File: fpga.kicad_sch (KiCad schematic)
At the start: 14 parts, among them U1 XC6SLX25-FTG256

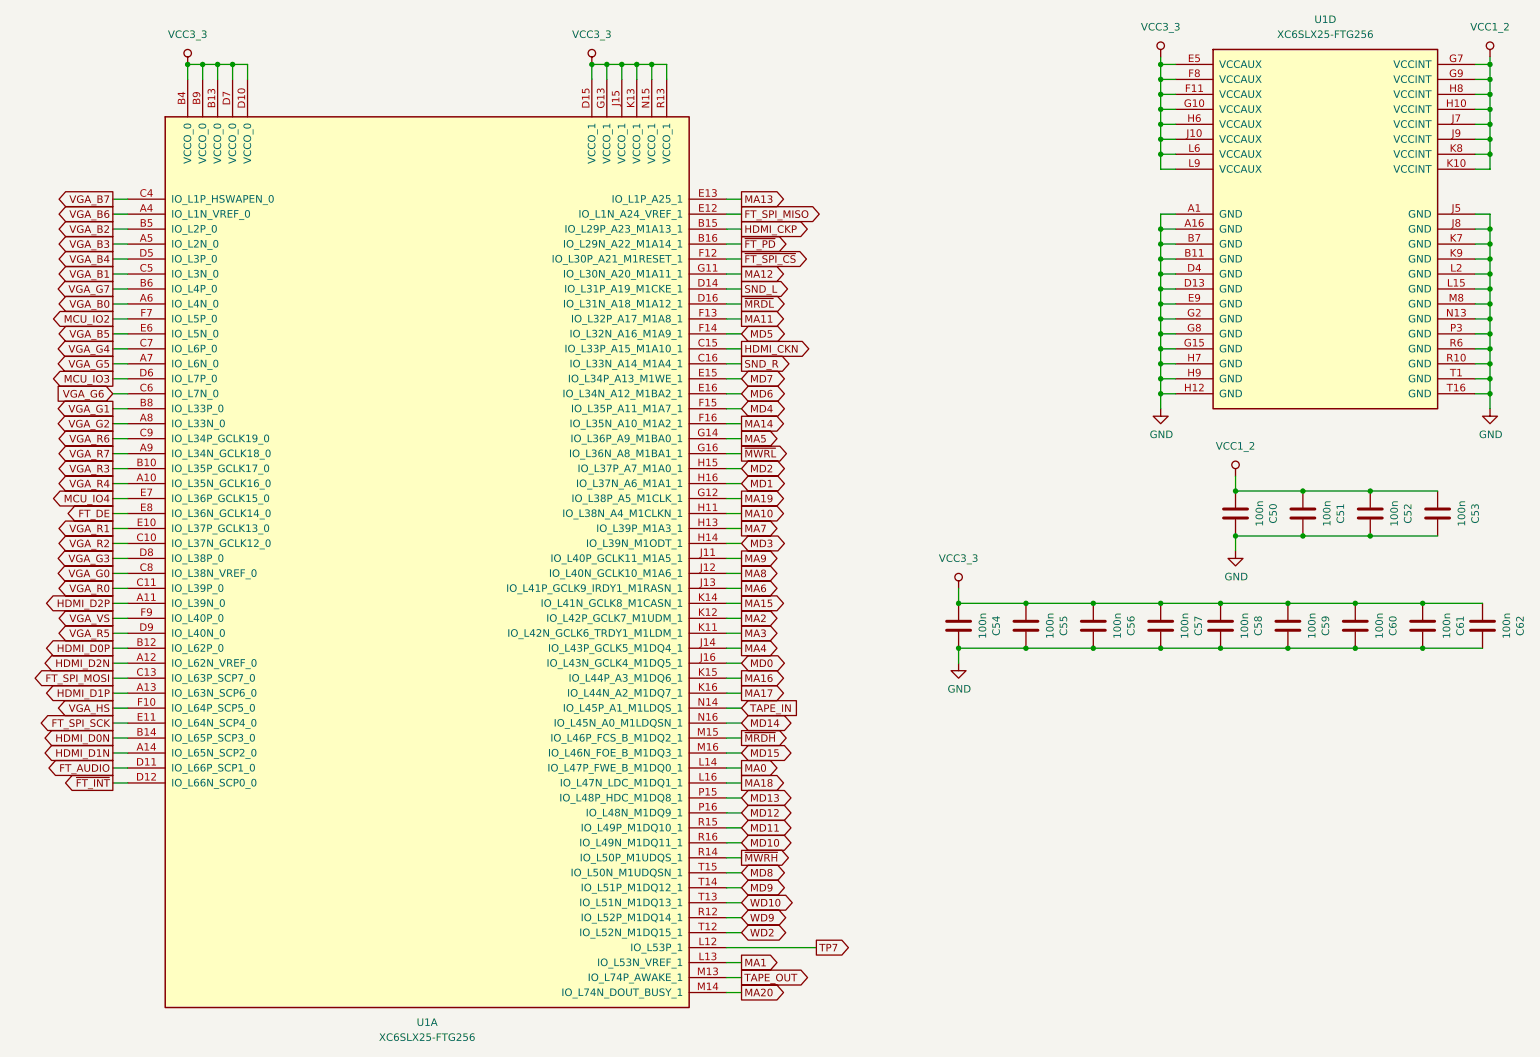
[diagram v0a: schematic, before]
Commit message: Updated revA: replaced resistors with IC for HDMI protection
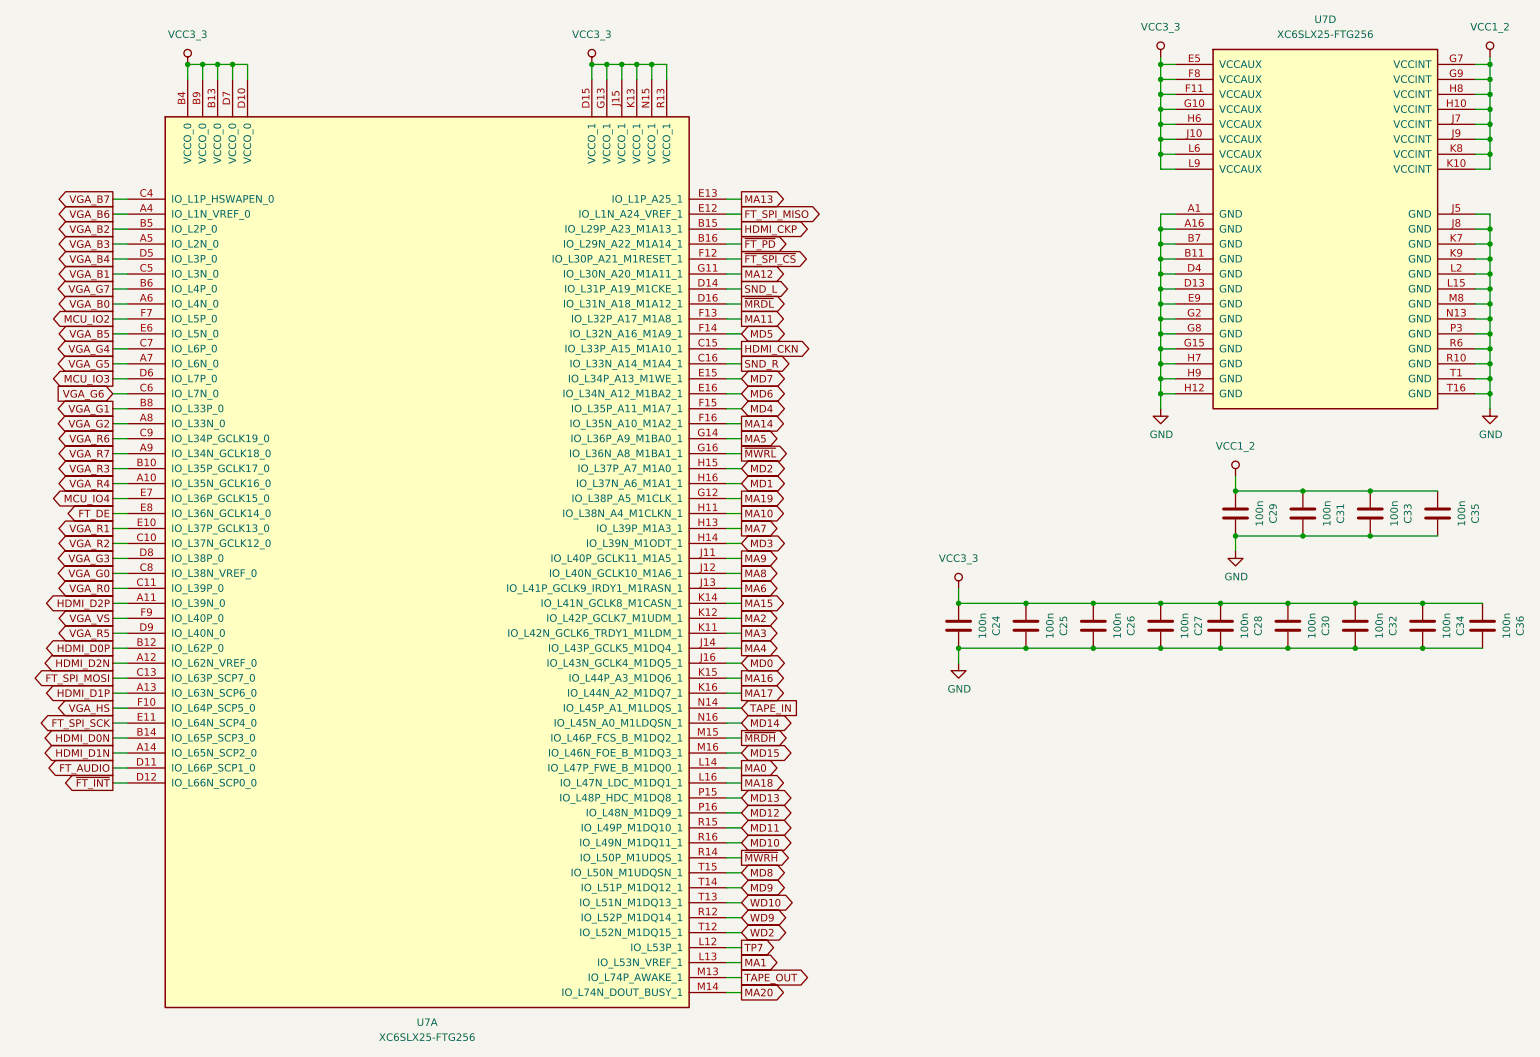
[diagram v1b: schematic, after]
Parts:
- renumbered C54 to C24, C55 to C25, C56 to C26, C57 to C27, C58 to C28, C50 to C29, C59 to C30, C51 to C31, C60 to C32, C52 to C33, C61 to C34, C53 to C35, C62 to C36, U1 to U7

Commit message: Cleanup revA
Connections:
- net TP7 renamed UBUS_11
- net WD10: no longer names the net of U7.T13 (IO_L51N_M1DQ13_1)
- net WD2 renamed UBUS_7
- net WD9 renamed UBUS_5
- no-connect marks 0 -> 1
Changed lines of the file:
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@@
   (junction (at 193.04 124.46) (diameter 0) (color 0 0 0 0)
   )
+  (no_connect (at 142.24 167.64))
   (wire (pts (xy 142.24 106.68) (xy 144.78 106.68))
     (stroke (width 0) (type default))
@@
     (stroke (width 0) (type default))
   )
-  (wire (pts (xy 142.24 167.64) (xy 144.78 167.64))
-    (stroke (width 0) (type default))
-  )
   (wire (pts (xy 271.78 55.88) (xy 271.78 58.42))
     (stroke (width 0) (type default))
@@
     (stroke (width 0) (type default))
   )
-  (global_label "MCU_IO2" (shape output) (at 38.1 68.58 180) (fields_autoplaced)
-    (effects (font (size 1.27 1.27)) (justify right))
-    (property "Intersheetrefs" "${INTERSHEET_REFS}" (at 26.9505 68.58 0)
+  (global_label "MCU_IO2" (shape bidirectional) (at 38.1 68.58 180) (fields_autoplaced)
+    (effects (font (size 1.27 1.27)) (justify right))
+    (property "Intersheetrefs" "${INTERSHEET_REFS}" (at 25.8392 68.58 0)
       (effects (font (size 1.27 1.27)) (justify right) hide)
     )
@@
     )
   )
-  (global_label "WD2" (shape bidirectional) (at 144.78 172.72 0) (fields_autoplaced)
-    (effects (font (size 1.27 1.27)) (justify left))
-    (property "Intersheetrefs" "${INTERSHEET_REFS}" (at 152.8074 172.72 0)
+  (global_label "UBUS_7" (shape bidirectional) (at 144.78 172.72 0) (fields_autoplaced)
+    (effects (font (size 1.27 1.27)) (justify left))
+    (property "Intersheetrefs" "${INTERSHEET_REFS}" (at 156.1941 172.72 0)
       (effects (font (size 1.27 1.27)) (justify left) hide)
     )
@@
     )
   )
-  (global_label "WD9" (shape bidirectional) (at 144.78 170.18 0) (fields_autoplaced)
-    (effects (font (size 1.27 1.27)) (justify left))
-    (property "Intersheetrefs" "${INTERSHEET_REFS}" (at 152.8074 170.18 0)
+  (global_label "UBUS_5" (shape bidirectional) (at 144.78 170.18 0) (fields_autoplaced)
+    (effects (font (size 1.27 1.27)) (justify left))
+    (property "Intersheetrefs" "${INTERSHEET_REFS}" (at 156.1941 170.18 0)
       (effects (font (size 1.27 1.27)) (justify left) hide)
     )
@@
     )
   )
-  (global_label "~{FT_INT}" (shape output) (at 38.1 147.32 180) (fields_autoplaced)
+  (global_label "~{FT_INT}" (shape input) (at 38.1 147.32 180) (fields_autoplaced)
     (effects (font (size 1.27 1.27)) (justify right))
     (property "Intersheetrefs" "${INTERSHEET_REFS}" (at 29.1881 147.32 0)
@@
     )
   )
-  (global_label "FT_AUDIO" (shape output) (at 38.1 144.78 180) (fields_autoplaced)
+  (global_label "FT_AUDIO" (shape input) (at 38.1 144.78 180) (fields_autoplaced)
     (effects (font (size 1.27 1.27)) (justify right))
     (property "Intersheetrefs" "${INTERSHEET_REFS}" (at 26.4666 144.78 0)
@@
     )
   )
-  (global_label "MCU_IO3" (shape output) (at 38.1 78.74 180) (fields_autoplaced)
-    (effects (font (size 1.27 1.27)) (justify right))
-    (property "Intersheetrefs" "${INTERSHEET_REFS}" (at 26.9505 78.74 0)
+  (global_label "MCU_IO3" (shape bidirectional) (at 38.1 78.74 180) (fields_autoplaced)
+    (effects (font (size 1.27 1.27)) (justify right))
+    (property "Intersheetrefs" "${INTERSHEET_REFS}" (at 25.8392 78.74 0)
       (effects (font (size 1.27 1.27)) (justify right) hide)
     )
@@
     )
   )
-  (global_label "FT_SPI_MISO" (shape output) (at 144.78 50.8 0) (fields_autoplaced)
+  (global_label "FT_SPI_MISO" (shape input) (at 144.78 50.8 0) (fields_autoplaced)
     (effects (font (size 1.27 1.27)) (justify left))
     (property "Intersheetrefs" "${INTERSHEET_REFS}" (at 159.4371 50.8 0)
@@
     )
   )
-  (global_label "TP7" (shape output) (at 144.78 175.26 0) (fields_autoplaced)
-    (effects (font (size 1.27 1.27)) (justify left))
-    (property "Intersheetrefs" "${INTERSHEET_REFS}" (at 151.2123 175.26 0)
-      (effects (font (size 1.27 1.27)) (justify left) hide)
-    )
-  )
-  (global_label "MCU_IO4" (shape output) (at 38.1 99.06 180) (fields_autoplaced)
-    (effects (font (size 1.27 1.27)) (justify right))
-    (property "Intersheetrefs" "${INTERSHEET_REFS}" (at 26.9505 99.06 0)
+  (global_label "UBUS_11" (shape bidirectional) (at 144.78 175.26 0) (fields_autoplaced)
+    (effects (font (size 1.27 1.27)) (justify left))
+    (property "Intersheetrefs" "${INTERSHEET_REFS}" (at 157.4036 175.26 0)
+      (effects (font (size 1.27 1.27)) (justify left) hide)
+    )
+  )
+  (global_label "MCU_IO4" (shape bidirectional) (at 38.1 99.06 180) (fields_autoplaced)
+    (effects (font (size 1.27 1.27)) (justify right))
+    (property "Intersheetrefs" "${INTERSHEET_REFS}" (at 25.8392 99.06 0)
       (effects (font (size 1.27 1.27)) (justify right) hide)
     )
@@
     )
   )
-  (global_label "WD10" (shape bidirectional) (at 144.78 167.64 0) (fields_autoplaced)
-    (effects (font (size 1.27 1.27)) (justify left))
-    (property "Intersheetrefs" "${INTERSHEET_REFS}" (at 154.0169 167.64 0)
-      (effects (font (size 1.27 1.27)) (justify left) hide)
-    )
-  )

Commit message: Updated revB
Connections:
- net UBUS_23: now reaches U7.T13 (IO_L51N_M1DQ13_1)
- no-connect marks 1 -> 0
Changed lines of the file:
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@@
   (title_block
     (title "Karabas-Mini")
-    (date "2024-02-20")
-    (rev "A")
+    (date "2024-02-23")
+    (rev "B")
   )
   (junction (at 129.54 25.4) (diameter 0) (color 0 0 0 0)
@@
   (junction (at 193.04 124.46) (diameter 0) (color 0 0 0 0)
   )
-  (no_connect (at 142.24 167.64))
   (wire (pts (xy 142.24 106.68) (xy 144.78 106.68))
     (stroke (width 0) (type default))
@@
   )
   (wire (pts (xy 129.54 25.4) (xy 132.08 25.4))
+    (stroke (width 0) (type default))
+  )
+  (wire (pts (xy 142.24 167.64) (xy 144.78 167.64))
     (stroke (width 0) (type default))
   )
@@
     )
   )
+  (global_label "UBUS_23" (shape bidirectional) (at 144.78 167.64 0) (fields_autoplaced)
+    (effects (font (size 1.27 1.27)) (justify left))
+    (property "Intersheetrefs" "${INTERSHEET_REFS}" (at 157.4036 167.64 0)
+      (effects (font (size 1.27 1.27)) (justify left) hide)
+    )
+  )

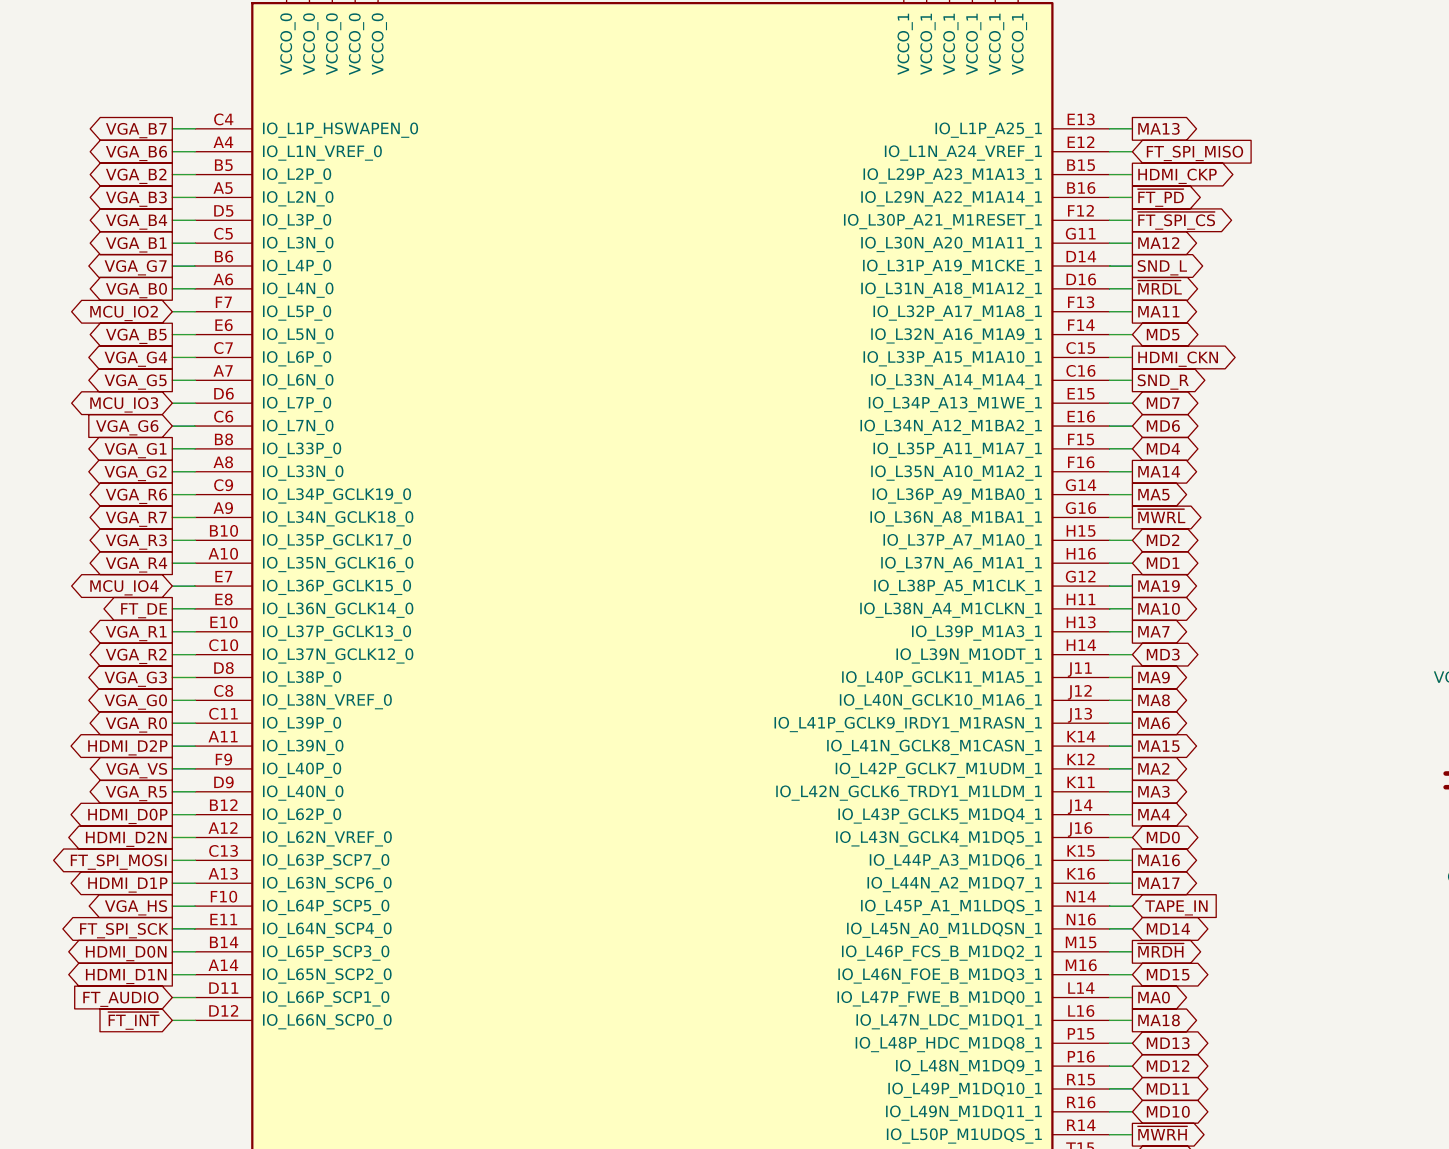
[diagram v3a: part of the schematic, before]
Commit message: Fixed HDMI diff-pairs pinout, rev.C
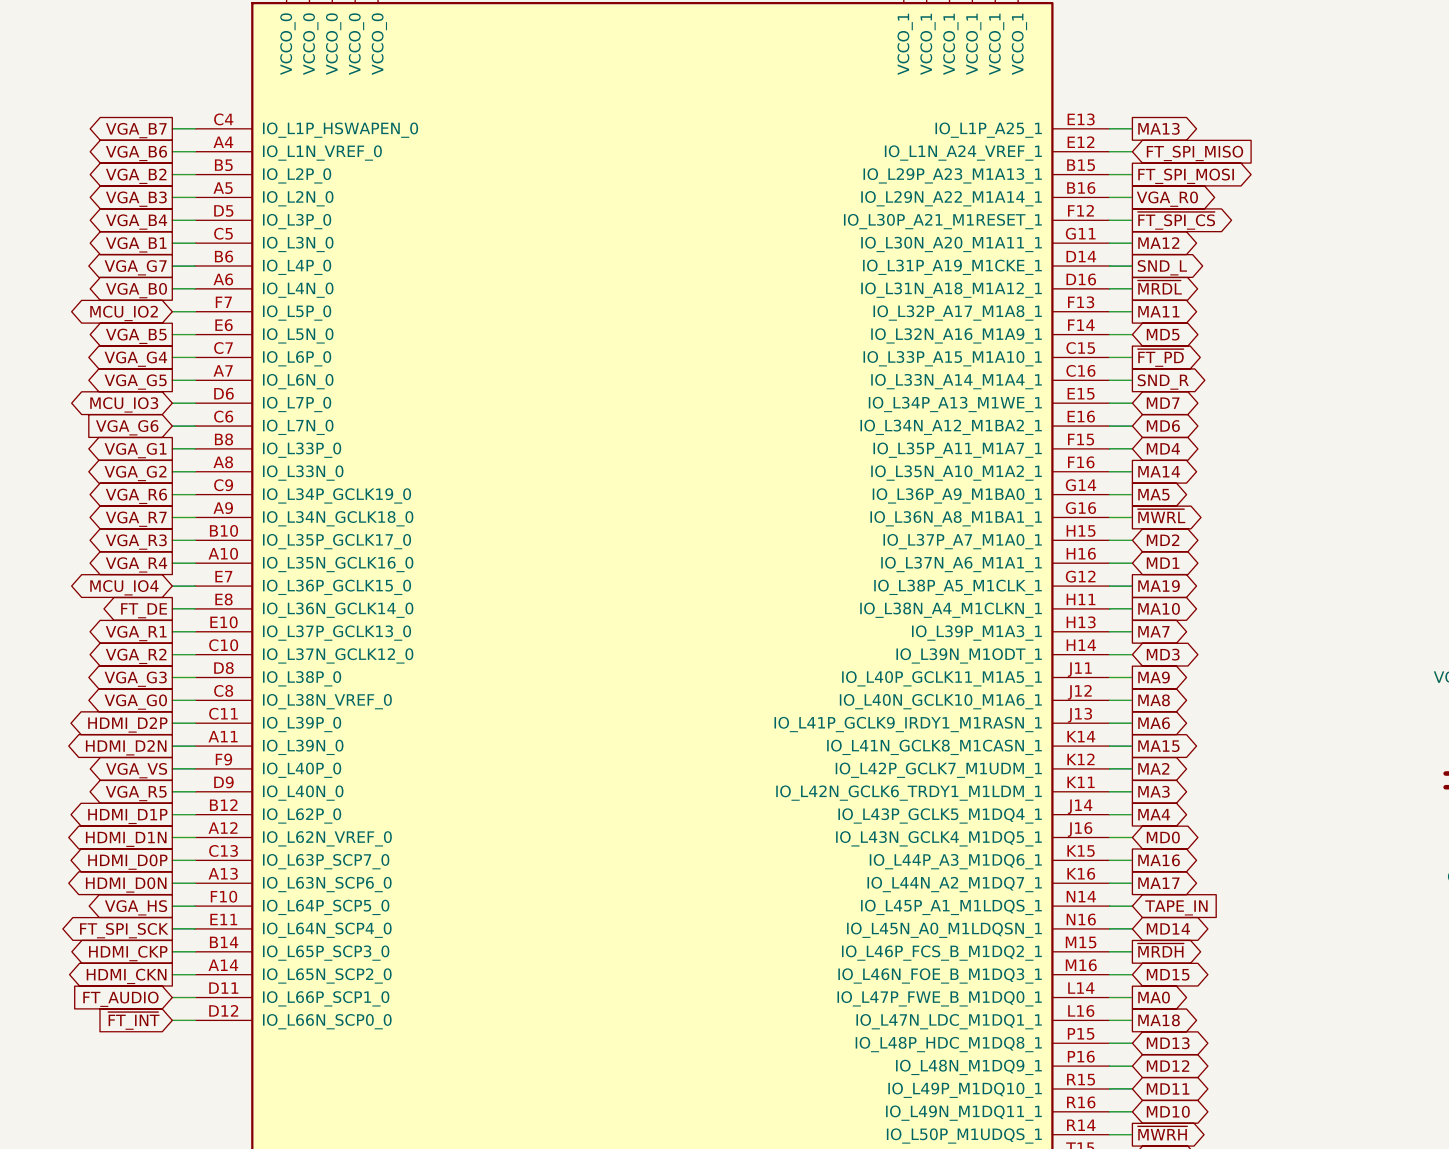
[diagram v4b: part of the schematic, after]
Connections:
- net FT_SPI_MOSI: now also U7.B15 (IO_L29P_A23_M1A13_1); no longer U7.C13 (IO_L63P_SCP7_0)
- net HDMI_CKN: now also U7.A14 (IO_L65N_SCP2_0); no longer U7.C15 (IO_L33P_A15_M1A10_1)
- net HDMI_CKP: now also U7.B14 (IO_L65P_SCP3_0); no longer U7.B15 (IO_L29P_A23_M1A13_1)
- net HDMI_D0N: now also U7.A13 (IO_L63N_SCP6_0); no longer U7.B14 (IO_L65P_SCP3_0)
- net HDMI_D0P: now also U7.C13 (IO_L63P_SCP7_0); no longer U7.B12 (IO_L62P_0)
- net HDMI_D1N: now also U7.A12 (IO_L62N_VREF_0); no longer U7.A14 (IO_L65N_SCP2_0)
- net HDMI_D1P: now also U7.B12 (IO_L62P_0); no longer U7.A13 (IO_L63N_SCP6_0)
- net HDMI_D2N: now also U7.A11 (IO_L39N_0); no longer U7.A12 (IO_L62N_VREF_0)
- net HDMI_D2P: now also U7.C11 (IO_L39P_0); no longer U7.A11 (IO_L39N_0)
- net VGA_R0: now also U7.B16 (IO_L29N_A22_M1A14_1); no longer U7.C11 (IO_L39P_0)
- net ~{FT_PD}: now also U7.C15 (IO_L33P_A15_M1A10_1); no longer U7.B16 (IO_L29N_A22_M1A14_1)

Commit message: revG
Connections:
- net FT_AUDIO renamed MCU_IO5
- net MCU_IO4 renamed FT_CLK_X
- net SND_L renamed DAC_DAT
- net SND_R renamed DAC_WS
- net VGA_R6 renamed MCU_SCK
- net VGA_R7 renamed FT_CLK
- net ~{FT_PD} renamed DAC_BCK
